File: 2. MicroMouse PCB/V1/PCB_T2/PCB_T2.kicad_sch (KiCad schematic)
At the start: 17 parts, among them U1 STM32F407VGTx, Y1 48MHz

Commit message: update PCB 12/08/2024
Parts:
- removed C10, C11: 20pF, Capacitor_SMD:C_0603_1608Metric, symbol Device:C_Polarized_Small
- removed L1: 10uH, Capacitor_SMD:C_0805_2012Metric_Pad1.18x1.45mm_HandSolder, symbol Device:L
- added C10, C11, C14, C15, C16: 100nF, Capacitor_SMD:C_0402_1005Metric, symbol Device:C
- added C12, C13: 15pF, Capacitor_SMD:C_0402_1005Metric, symbol Device:C
- added D0, D1, D2, D3: 3VL, LED_SMD:LED_0603_1608Metric, symbol Device:LED
- added J1: MPU, Connector_PinHeader_2.54mm:PinHeader_1x04_P2.54mm_Vertical, symbol Connector:Conn_01x04_Socket
- added J10: Conn_01x26_Socket, Connector_FFC-FPC:Hirose_FH12-26S-0.5SH_1x26-1MP_P0.50mm_Horizontal, symbol Connector:Conn_01x26_Socket
- added J2, J3, J4: MPU, Connector_JST:JST_SH_BM04B-SRSS-TB_1x04-1MP_P1.00mm_Vertical, symbol Connector:Conn_01x04_Socket
- added J5: Conn_01x04_Pin, symbol Connector:Conn_01x04_Pin
- added J6, J7, J8, J9: Conn_01x03_Pin, Connector_JST:JST_SH_BM03B-SRSS-TB_1x03-1MP_P1.00mm_Vertical, symbol Connector:Conn_01x03_Pin
- added R1, R2: 1K, Resistor_SMD:R_0402_1005Metric, symbol Device:R
- added RN1: R_Pack04, Resistor_SMD:R_Array_Convex_4x0603, symbol Device:R_Pack04
- added SW1, SW2, SW3: SW_Push, Button_Switch_SMD:SW_Tactile_SPST_NO_Straight_CK_PTS636Sx25SMTRLFS, symbol Switch:SW_Push
- added U2: Output 3.3V, Mini560:Mini560_5A, symbol Mini560-5A:Mini560-5A
- C1, C3: value 100nF -> 2.2uF; footprint Capacitor_SMD:C_0603_1608Metric -> Capacitor_Tantalum_SMD:CP_EIA-3216-10_Kemet-I
- C2, C4, C5, C6, C7, C8: footprint Capacitor_SMD:C_0603_1608Metric -> Capacitor_SMD:C_0402_1005Metric
- C9: value 100nF -> 4.7uF; footprint Capacitor_SMD:C_0603_1608Metric -> Capacitor_Tantalum_SMD:CP_EIA-3216-10_Kemet-I
- R3, R4: footprint Resistor_SMD:R_0603_1608Metric -> Resistor_SMD:R_0402_1005Metric
- STLINK1: renamed from UART1; footprint JST254:JST 4 -> Connector_JST:JST_SH_SM04B-SRSS-TB_1x04-1MP_P1.00mm_Horizontal
- U1: value STM32F407VGTx -> STM32H743VIT6
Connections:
- net VCC is gone; now on net +3.3V: R3.2
- net +3.3V: now also C2.2, C6.1, U1.21 (VREF+), U1.6 (VBAT), C10.2, C11.1, C15.2, C16.2, J1.1 (Pin_1), J2.1 (Pin_1), J3.1 (Pin_1), J4.1 (Pin_1), R1.2, R2.2, U2. (OUT-); no longer C2.1
- net +5V: now also J5.3 (Pin_3), J6.2 (Pin_2), J7.2 (Pin_2), J8.2 (Pin_2), J9.2 (Pin_2)
- net GND: now also C2.1, C6.2, R4.1, C10.1, C11.2, C12.1, C13.1, C14.1, C15.1, C16.1, J1.4 (Pin_4), J2.4 (Pin_4), J3.4 (Pin_4), J4.4 (Pin_4), J5.4 (Pin_4), J6.3 (Pin_3), J7.3 (Pin_3), J8.3 (Pin_3), J9.3 (Pin_3), RN1.5 (R4.2), RN1.6 (R3.2), RN1.7 (R2.2), RN1.8 (R1.2), SW1.1, SW2.1, SW3.1, U2. (OUT-); no longer C6.1, R4.2
- net I2C1_SCL: now also J4.2 (Pin_2)
- net I2C1_SDA: now also J4.3 (Pin_3)
- net NE_IN1: now also J10.20 (Pin_20)
- net NE_IN2: now also J10.21 (Pin_21)
- net NE_PWM: now also J10.22 (Pin_22)
- net NRST: now also C14.2, SW1.2
- net NW_ENC_A: now also J10.8 (Pin_8)
- net NW_ENC_B: now also J10.9 (Pin_9)
- net NW_IN1: now also J10.5 (Pin_5)
- net NW_IN2: now also J10.6 (Pin_6)
- net NW_PWM: now also J10.7 (Pin_7)
- net PH0: now also C12.2
- net PH1: now also C13.2
- net SE_ENC_A: now also J10.18 (Pin_18)
- net SE_ENC_B: now also J10.19 (Pin_19)
- net SE_IN1: now also J10.15 (Pin_15)
- net SE_IN2: now also J10.16 (Pin_16)
- net SE_PWM: now also J10.17 (Pin_17)
- net SWDIO: now also R4.2; no longer R4.1
- net SW_ENC_A: now also J10.13 (Pin_13)
- net SW_ENC_B: now also J10.14 (Pin_14)
- net SW_IN1: now also J10.10 (Pin_10)
- net SW_IN2: now also J10.11 (Pin_11)
- net SW_PWM: now also J10.12 (Pin_12)
- net USART1_RX: now also J1.3 (Pin_3)
- net USART1_TX: now also J1.2 (Pin_2)
- net USART2_RX: now also J2.3 (Pin_3)
- net USART2_TX: now also J2.2 (Pin_2)
- net USART3_RX: now also J3.3 (Pin_3)
- net USART3_TX: now also J3.2 (Pin_2)
- net N_TOF: now reaches U1.15 (PC0)
- net N_TOF: now also J10.1 (Pin_1)
- net W_TOF: now reaches U1.16 (PC1)
- net W_TOF: now also J10.2 (Pin_2)
- net S_TOF: now reaches U1.17 (PC2)
- net S_TOF: now also J10.3 (Pin_3)
- net E_TOF: now reaches U1.18 (PC3)
- net E_TOF: now also J10.4 (Pin_4)
- net NE_ENC_A: now reaches U1.23 (PA0)
- net NE_ENC_A: now also J10.23 (Pin_23)
- net NE_ENC_B: now reaches U1.24 (PA1)
- net NE_ENC_B: now also J10.24 (Pin_24)
- net BUTTON_0: now reaches U1.81 (PD0)
- net BUTTON_1: now reaches U1.82 (PD1)
- net BUTTON_1: now also R1.1, SW2.2
- net LED_0: now reaches U1.83 (PD2)
- net LED_0: now also D0.2 (A)
- net LED_1: now reaches U1.84 (PD3)
- net LED_1: now also D1.2 (A)
- net LED_2: now reaches U1.85 (PD4)
- net LED_2: now also D2.2 (A)
- net LED_3: now reaches U1.86 (PD5)
- net LED_3: now also D3.2 (A)
- net E_52_EXTI: no longer names the net of U1.51 (PB12)
- net E_53_XSHUT: no longer names the net of U1.52 (PB13)
- net E_61_EXTI: no longer names the net of U1.57 (PD10)
- net E_61_XSHUT: no longer names the net of U1.58 (PD11)
- net N_53_EXTI: no longer names the net of U1.70 (PA11)
- net N_53_XSHUT: no longer names the net of U1.69 (PA10)
- net N_61_EXTI: no longer names the net of U1.77 (PA15)
- net N_61_XSHUT: no longer names the net of U1.71 (PA12)
- net S_53_EXTI: no longer names the net of U1.61 (PD14)
- net S_53_XSHUT: no longer names the net of U1.62 (PD15)
- net S_61_EXTI renamed NW_SERVO
- net NW_SERVO: now also J6.1 (Pin_1)
- net S_61_XSHUT renamed SW_SERVO
- net SW_SERVO: now also J7.1 (Pin_1)
- net W_53_EXTI renamed NE_SERVO
- net NE_SERVO: now also J9.1 (Pin_1)
- net W_53_XSHUT renamed SE_SERVO
- net SE_SERVO: now also J8.1 (Pin_1)
- net W_61_EXTI: no longer names the net of U1.67 (PA8)
- net W_61_XSHUT: no longer names the net of U1.68 (PA9)
- new net: D3.1 (K), RN1.4 (R4.1)
- new net: J5.1 (Pin_1), U2. (OUT-)
- new net: J5.2 (Pin_2), U2. (OUT-)
- new net: D0.1 (K), RN1.1 (R1.1)
- new net: D1.1 (K), RN1.2 (R2.1)
- new net: D2.1 (K), RN1.3 (R3.1)
- new net BUTTON_2: R2.1, SW3.2
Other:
- note added: "ESP32 DISPLAY"
- note added: "EXTERNAL I2C"
- note added: "EXTERNAL UART"
- note added: "LED DEBUG"
- note added: "MPU SENSOR"
- note added: "POWER SOURCE"
- note added: "RESET BUTTON"
- note added: "SERVO"
- note added: "USER BUTTON"
- moved on the sheet: C1, C2, C3, C4, C5, C7, C8, C9, R3, R4, STLINK1, U1

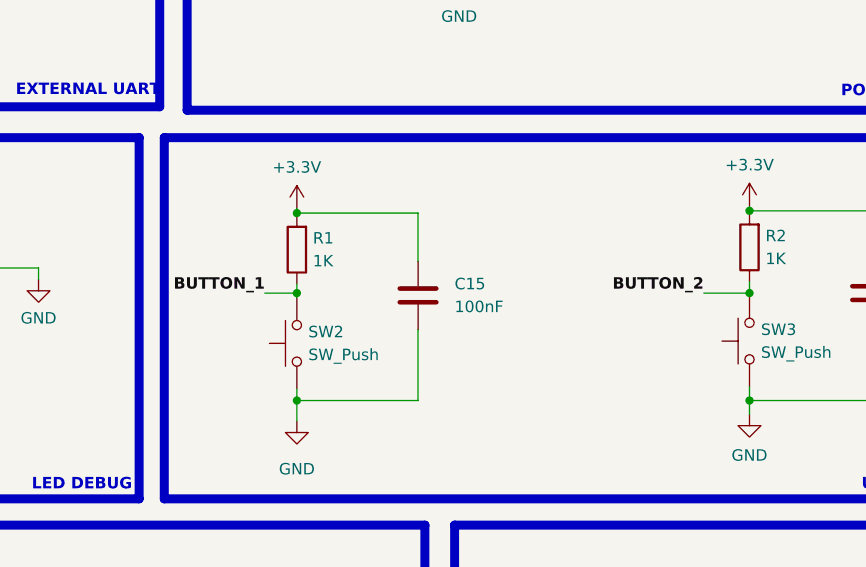
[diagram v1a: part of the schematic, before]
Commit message: update route tracks before change
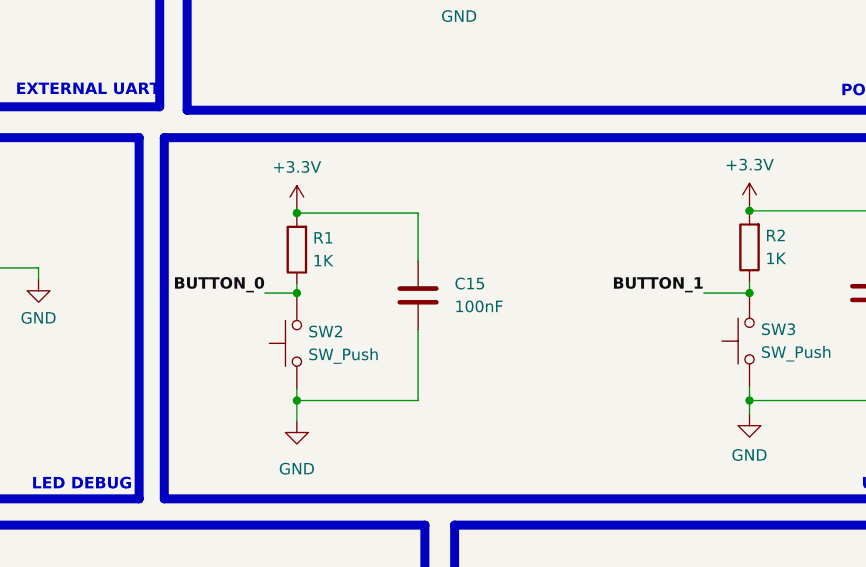
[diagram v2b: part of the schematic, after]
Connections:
- net BUTTON_2 is gone; now on net BUTTON_1: R2.1, SW3.2
- net BUTTON_0: now also R1.1, SW2.2
- net BUTTON_1: no longer R1.1, SW2.2
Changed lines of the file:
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@@
 		)
 	)
-	(label "BUTTON_1"
+	(label "BUTTON_0"
 		(at 325.374 120.904 180)
 		(fields_autoplaced yes)
@@
 		)
 	)
-	(label "BUTTON_2"
+	(label "BUTTON_1"
 		(at 374.142 120.904 180)
 		(fields_autoplaced yes)

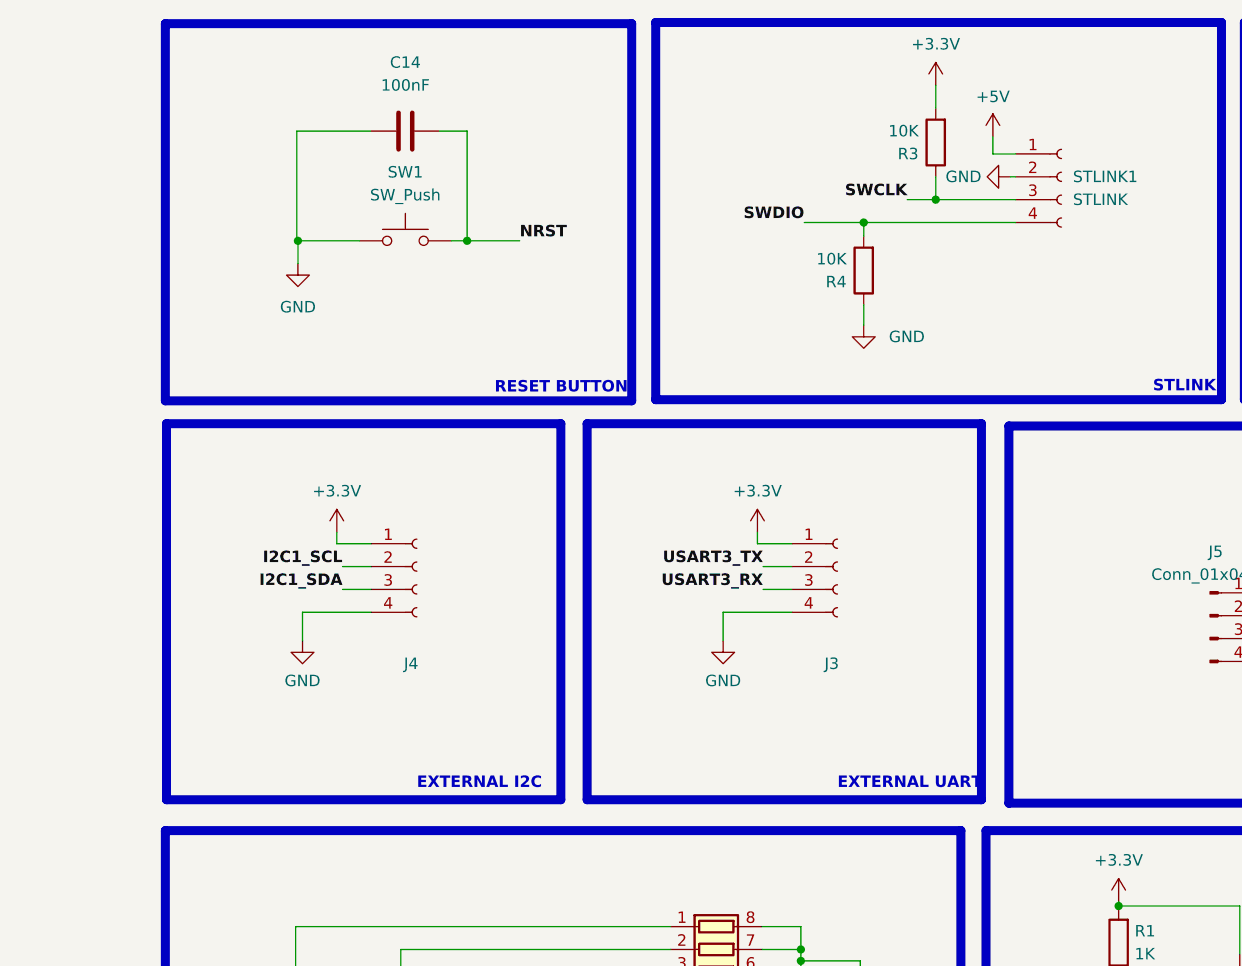
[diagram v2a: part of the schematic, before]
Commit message: completed schematic of all in one PCB
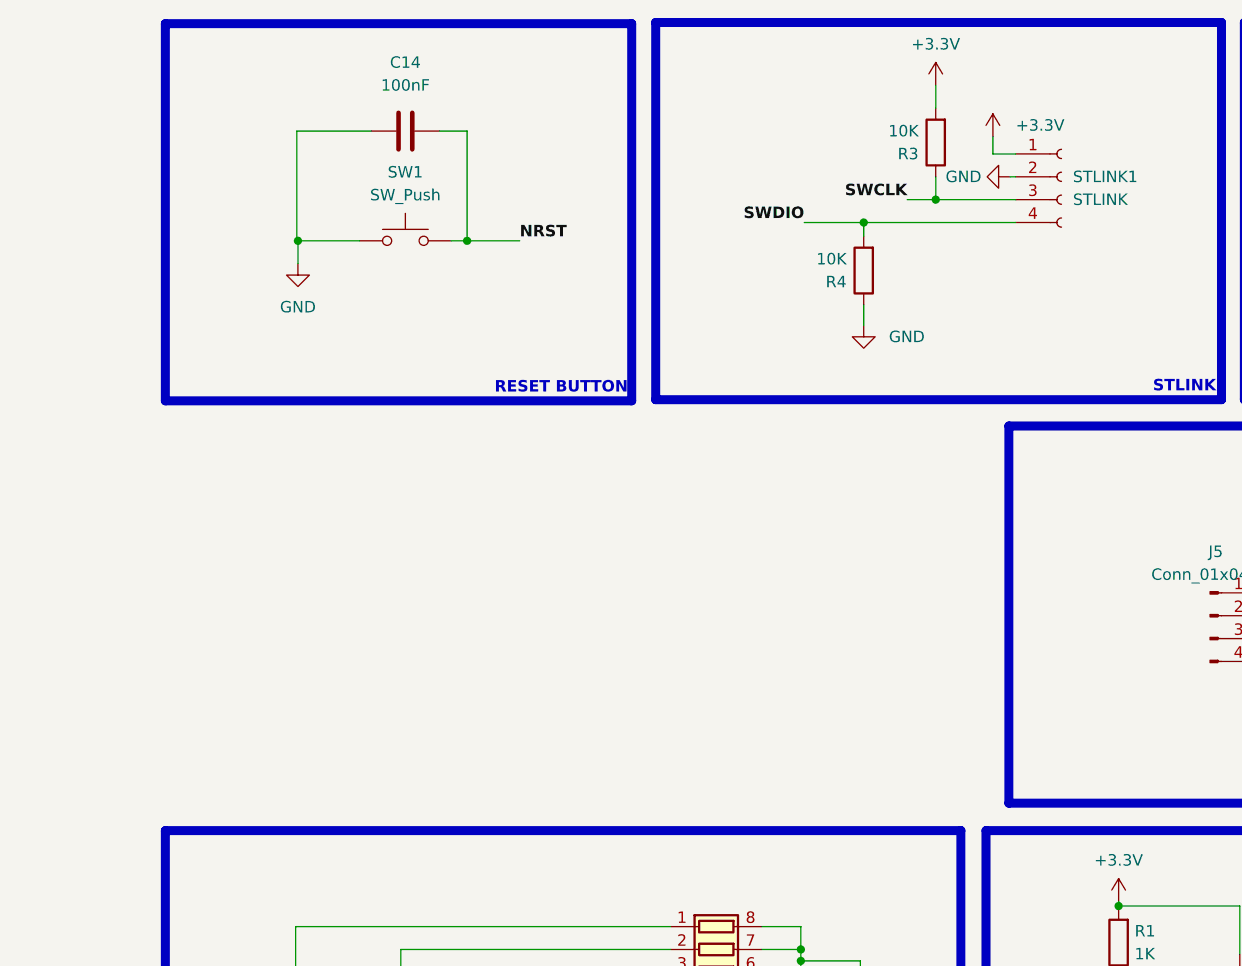
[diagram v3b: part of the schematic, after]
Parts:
- removed J3, J4: MPU, Connector_JST:JST_SH_BM04B-SRSS-TB_1x04-1MP_P1.00mm_Vertical, symbol Connector:Conn_01x04_Socket
- J5: footprint (none) -> Connector_PinHeader_2.54mm:PinHeader_1x04_P2.54mm_Vertical
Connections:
- net +3.3V: now also STLINK1.1 (Pin_1)
- net +5V: no longer STLINK1.1 (Pin_1)
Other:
- note removed: "EXTERNAL I2C"
- note removed: "EXTERNAL UART"
